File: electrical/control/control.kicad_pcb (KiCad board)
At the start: 2 copper layers, 43 parts, among them J1 USB4105-GF-A, J2 SWD, J3 TC2030-NL, J4 UART, J5 QWIIC, SW1 SYS, U1 USBLC6-2P6, U2 LP5912-3.3DRV, U3 W25Q16JVSSIQ, U4 RP2040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

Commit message: More PCB layout
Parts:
- U3: value W25Q16JVSSIQ -> W25Q16JVSNIQ; footprint Package_SO:SOIC-8_5.3x5.3mm_P1.27mm -> Package_SO:SOIC-8_3.9x4.9mm_P1.27mm
- moved J5 37.9 mm to (167.8, 82.8)
- moved U5 33.3 mm to (166.6, 95.8)
- moved C18 33.3 mm to (166.1, 88.8)
- moved R8 30.6 mm to (161.4, 74.3), turned to 90 degrees
- moved H1 30.0 mm to (137.6, 95.4)
- moved D1 29.2 mm to (161.6, 68.8)
- moved J2 25.7 mm to (135.8, 71.2)
- moved J4 25.0 mm to (142.7, 71.2)
- moved J3 23.4 mm to (136.6, 81.5)
- moved SW1 21.4 mm to (168.8, 71.4)
- moved C15 12.2 mm to (143.9, 78.2), turned to 90 degrees
- moved Y1 7.10 mm to (147.8, 99.4), turned to -90 degrees
- moved C16 6.67 mm to (150.0, 98.6), turned to 90 degrees
- moved U3 6.53 mm to (145.8, 83.0), turned to 90 degrees
- moved C17 3.81 mm to (150.0, 100.6), turned to -90 degrees
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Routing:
- net +3.3V: track 18.2 -> 59.2 mm
- net GND: track 15.6 -> 44.4 mm, vias 11 -> 20
- net /QSPI_SD3: track 0.00 -> 16.0 mm
- net /QSPI_SCLK: track 0.00 -> 13.8 mm
- net /QSPI_SD0: track 0.00 -> 9.72 mm
- net /QSPI_SS: track 0.00 -> 7.59 mm
- net /QSPI_SD1: track 0.00 -> 6.82 mm
- net /QSPI_SD2: track 0.00 -> 5.93 mm
- net Net-(U4-XIN): track 2.94 -> 7.61 mm
- net Net-(C17-Pad1): track 0.00 -> 2.51 mm
- net Net-(U4-XOUT): track 2.50 -> 3.70 mm
- net Net-(U4-GPIO1): track 2.98 -> 1.90 mm
- net Net-(U4-GPIO0): track 2.65 -> 1.65 mm
- net Net-(U4-SWCLK): track 6.05 -> 5.40 mm
- net Net-(U4-SWD): track 5.03 -> 4.47 mm
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- added copper zone on B.Cu, net GND

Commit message: More PCB work
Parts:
- U3: value W25Q16JVSNIQ -> W25Q16JVUXIQ; footprint Package_SO:SOIC-8_3.9x4.9mm_P1.27mm -> Package_SON:Winbond_USON-8-1EP_3x2mm_P0.5mm_EP0.2x1.6mm
- moved J4 39.1 mm to (166.7, 102.1), turned to 90 degrees
- moved J2 39.1 mm to (166.7, 95.1), turned to 90 degrees
- moved H1 32.1 mm to (166.6, 81.6)
- moved J3 30.7 mm to (166.5, 88.2), turned to 0 degrees
- moved J5 27.8 mm to (164.5, 110.4), turned to 0 degrees
- moved C18 21.7 mm to (159.0, 109.3), turned to 90 degrees
- moved U5 20.2 mm to (152.0, 109.7), turned to -90 degrees
- moved R8 17.7 mm to (157.0, 91.4), turned to 0 degrees
- moved R4 12.7 mm to (157.0, 96.6)
- moved R5 11.7 mm to (157.0, 95.6)
- moved C15 5.60 mm to (145.4, 83.6), turned to -90 degrees
- moved D1 3.50 mm to (162.8, 72.1)
- moved R10 3.01 mm to (154.0, 98.6), turned to -90 degrees
- moved R11 2.33 mm to (155.0, 98.6), turned to -90 degrees
- moved SW1 2.30 mm to (171.0, 70.8)
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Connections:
- R4 pad 1: UART_TX -> Net-(U4-GPIO16)
- R4 pad 2: Net-(U4-GPIO0) -> UART_TX
- R5 pad 1: UART_RX -> Net-(U4-GPIO17)
- R5 pad 2: Net-(U4-GPIO1) -> UART_RX
- R8 pad 1: Net-(U4-GPIO2) -> Net-(U4-GPIO25)
- SW1 pad 1: Net-(U4-GPIO3) -> Net-(U4-GPIO24)
- U4 pad 12: unconnected-(U4-GPIO9-Pad12) -> PRESSURE_INT
- U4 pad 13: unconnected-(U4-GPIO10-Pad13) -> I2C_SDA
- U4 pad 14: unconnected-(U4-GPIO11-Pad14) -> I2C_SCL
- U4 pad 2: Net-(U4-GPIO0) -> unconnected-(U4-GPIO0-Pad2)
- U4 pad 27: unconnected-(U4-GPIO16-Pad27) -> Net-(U4-GPIO16)
- U4 pad 28: unconnected-(U4-GPIO17-Pad28) -> Net-(U4-GPIO17)
- U4 pad 3: Net-(U4-GPIO1) -> unconnected-(U4-GPIO1-Pad3)
- U4 pad 36: unconnected-(U4-GPIO24-Pad36) -> Net-(U4-GPIO24)
- U4 pad 37: unconnected-(U4-GPIO25-Pad37) -> Net-(U4-GPIO25)
- U4 pad 38: I2C_SCL -> unconnected-(U4-GPIO26_ADC0-Pad38)
- U4 pad 39: I2C_SDA -> unconnected-(U4-GPIO27_ADC1-Pad39)
- U4 pad 4: Net-(U4-GPIO2) -> unconnected-(U4-GPIO2-Pad4)
- U4 pad 40: PRESSURE_INT -> unconnected-(U4-GPIO28_ADC2-Pad40)
- U4 pad 5: Net-(U4-GPIO3) -> unconnected-(U4-GPIO3-Pad5)
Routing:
- net I2C_SDA: track 0.00 -> 46.7 mm
- net +3.3V: track 59.2 -> 99.7 mm, vias 0 -> 4
- net I2C_SCL: track 0.00 -> 38.5 mm
- net PRESSURE_INT: track 0.00 -> 33.7 mm
- net Net-(U4-GPIO24): track 0.00 -> 21.1 mm
- net Net-(D1-A): track 0.00 -> 18.5 mm
- net +1V1: track 8.33 -> 20.5 mm, vias 0 -> 3
- net /QSPI_SD3: track 16.0 -> 10.6 mm
- net GND: track 44.4 -> 49.4 mm, vias 20 -> 24
- net /QSPI_SCLK: track 13.8 -> 9.16 mm
- net Net-(U4-GPIO16): track 0.00 -> 3.22 mm
- net /QSPI_SS: track 7.59 -> 4.58 mm
- net /QSPI_SD0: track 9.72 -> 6.85 mm
- net Net-(U4-SWCLK): track 5.40 -> 2.95 mm
- net /QSPI_SD1: track 6.82 -> 4.48 mm
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- added copper zone on F.Cu, net +3.3V

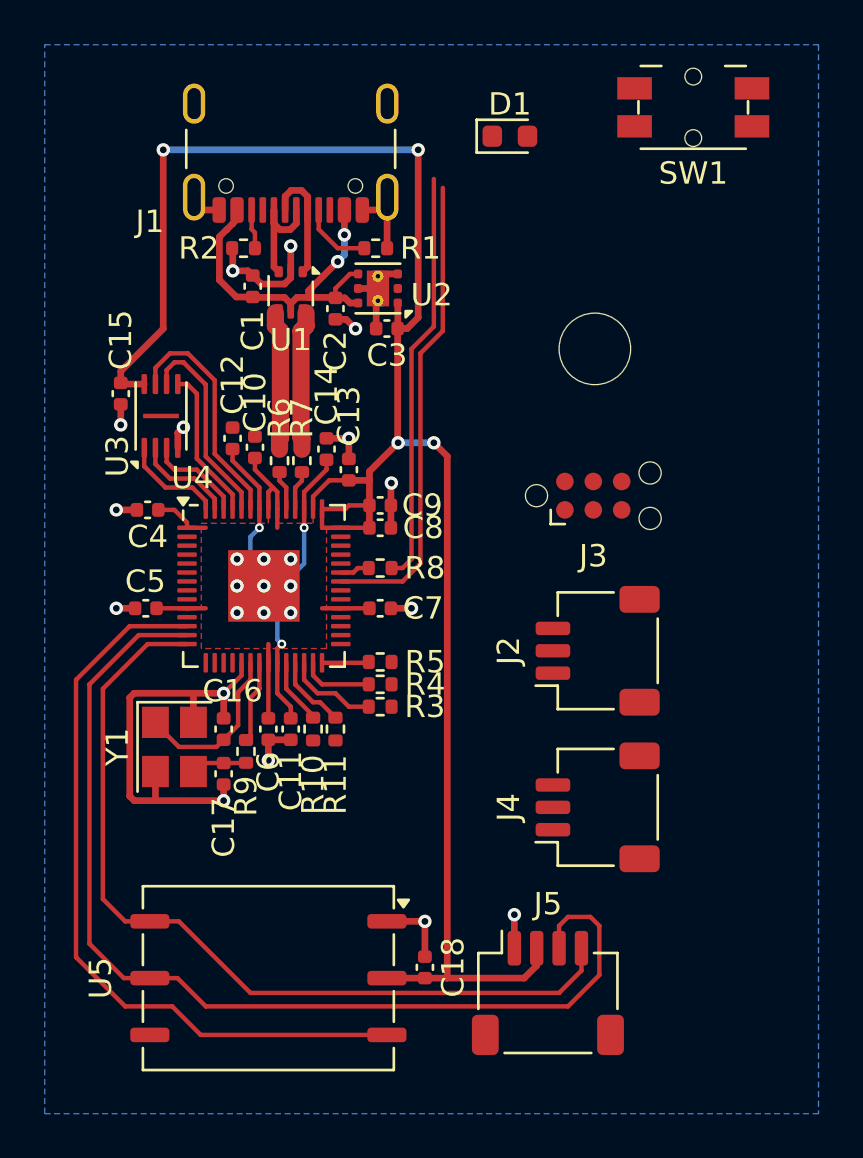
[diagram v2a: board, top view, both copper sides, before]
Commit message: All nets routed for control board
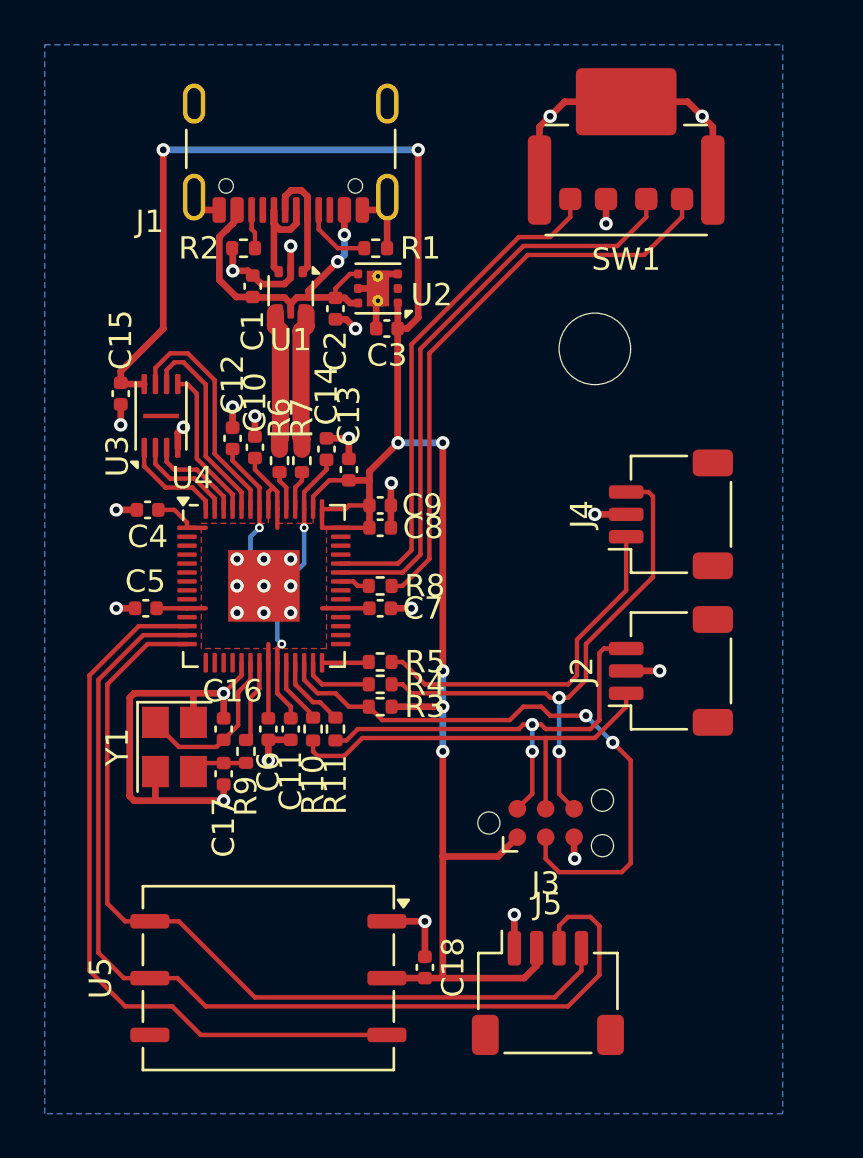
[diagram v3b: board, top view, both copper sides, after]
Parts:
- removed D1: RED, LED_SMD:LED_0603_1608Metric
- SW1: value SYS -> 228EMSARGFR; footprint Button_Switch_SMD:Panasonic_EVQPUL_EVQPUC -> midi_concertina:CTS_228EMS
- moved J3 14.8 mm to (164.4, 102.8)
- moved J4 13.5 mm to (170.0, 89.0)
- moved SW1 5.08 mm to (168.0, 74.9), turned to 180 degrees
- moved J2 3.40 mm to (170.0, 96.0)
- moved R8 0.80 mm to (157.0, 92.2)
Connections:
- R8 pad 1: Net-(U4-GPIO25) -> Net-(U4-GPIO24)
- R8 pad 2: Net-(D1-A) -> Net-(R8-Pad2)
- U4 pad 38: unconnected-(U4-GPIO26_ADC0-Pad38) -> Net-(U4-GPIO26_ADC0)
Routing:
- net Net-(R8-Pad2): track 0.00 -> 26.0 mm
- net UART_TX: track 0.00 -> 25.2 mm, vias 0 -> 2
- net Net-(U4-GPIO25): track 1.34 -> 26.4 mm
- net RUN: track 4.15 -> 27.1 mm, vias 0 -> 2
- net Net-(U4-GPIO26_ADC0): track 0.00 -> 22.9 mm
- net SWDIO: track 0.00 -> 20.7 mm, vias 0 -> 2
- net GND: track 49.4 -> 69.6 mm, vias 24 -> 32
- net Net-(U4-GPIO24): track 21.1 -> 1.34 mm
- net SWCLK: track 0.00 -> 19.2 mm
- net Net-(D1-A): track 18.5 -> 0.00 mm
- net UART_RX: track 0.00 -> 16.0 mm
- net +3.3V: track 99.7 -> 105.9 mm, vias 4 -> 7
- net PRESSURE_INT: track 33.7 -> 33.0 mm

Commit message: Fix various DRC errors
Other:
- board outline added: 33 x 48 mm
- rule solder_mask_min_width: 0.2 -> 0.1
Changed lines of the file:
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@@
 		)
 		(pad_to_mask_clearance 0.038)
-		(solder_mask_min_width 0.2)
+		(solder_mask_min_width 0.1)
 		(allow_soldermask_bridges_in_footprints no)
 		(tenting front back)
@@
 		)
 	)
+	(gr_rect
+		(start 142 68)
+		(end 175 116)
+		(stroke
+			(width 0.05)
+			(type default)
+		)
+		(fill no)
+		(layer "Edge.Cuts")
+	)
 	(segment
 		(start 155.65 78.25)
@@
 		(polygon
 			(pts
-				(xy 142 68) (xy 175 68) (xy 175 115.8) (xy 142 115.8)
+				(xy 142 68) (xy 175 68) (xy 175 116) (xy 142 116)
 			)
 		)

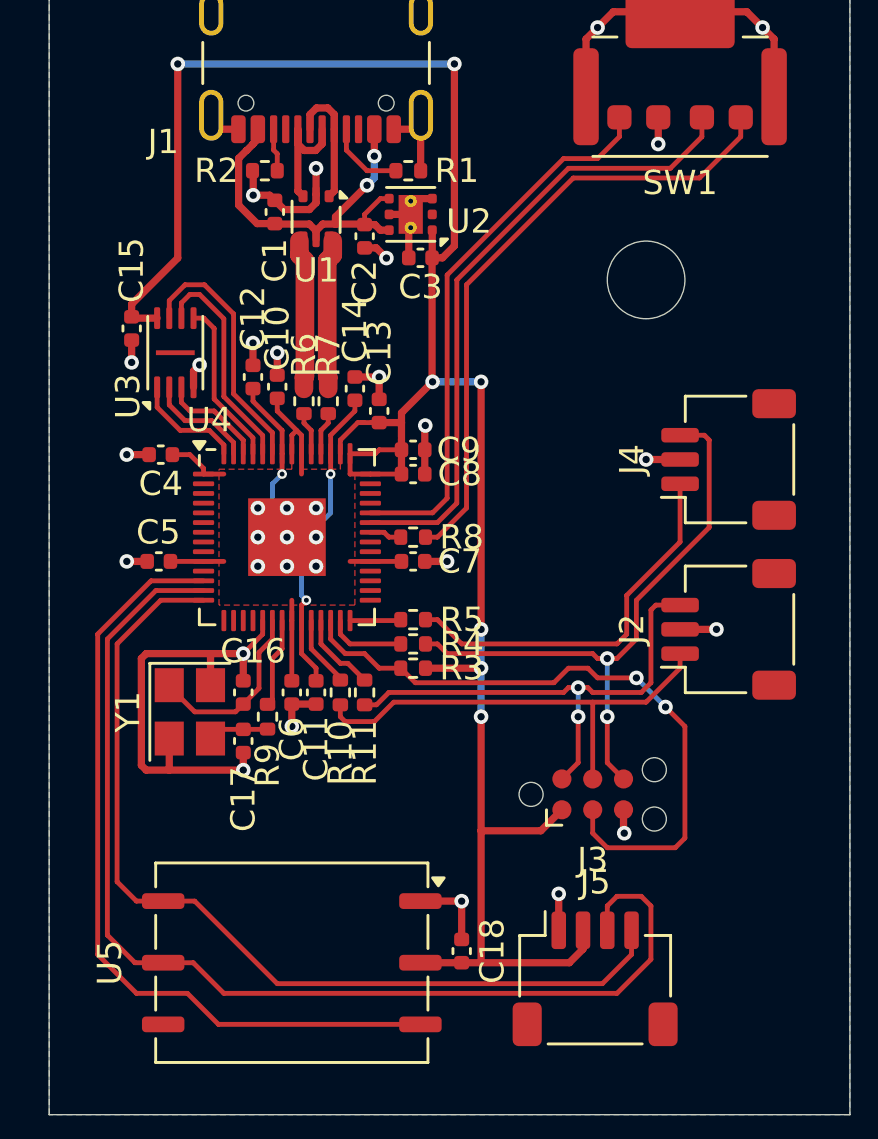
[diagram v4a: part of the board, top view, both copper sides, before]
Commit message: Clean up silkscreen
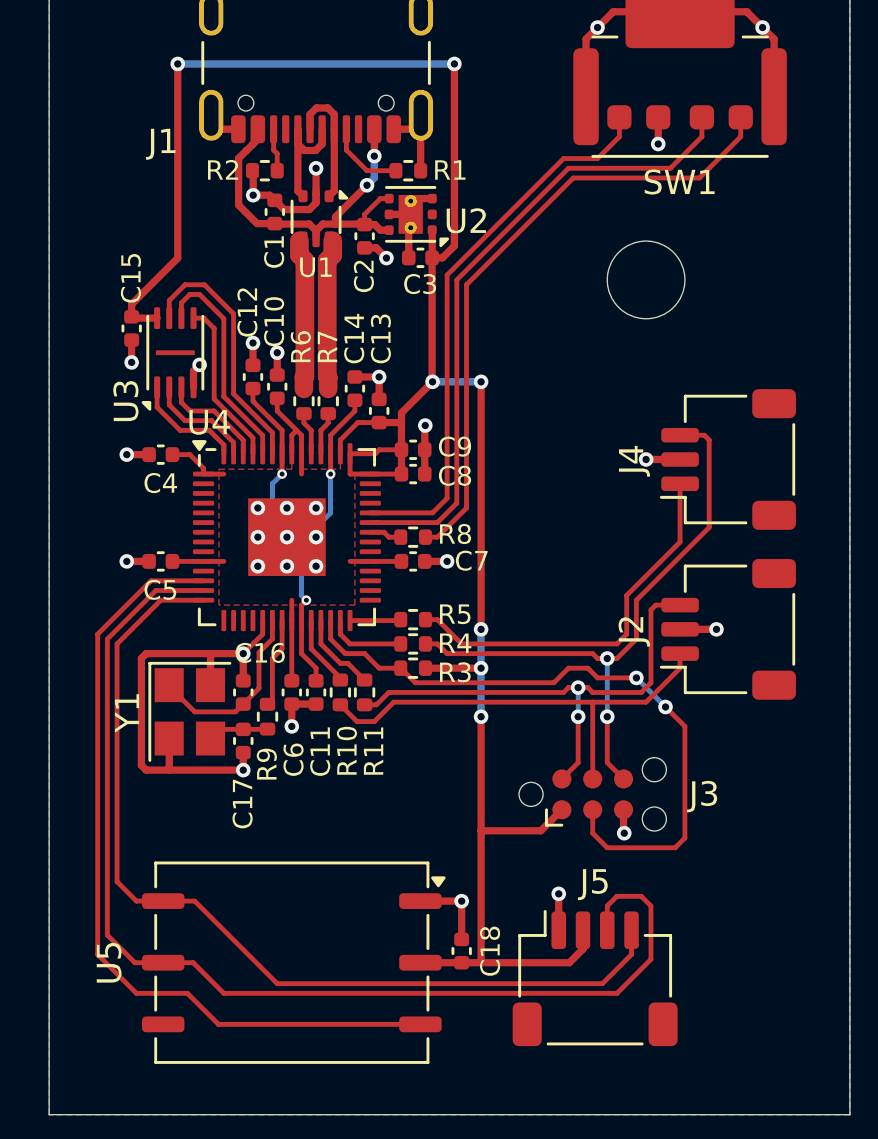
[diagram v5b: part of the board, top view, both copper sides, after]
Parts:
- moved C5 0.08 mm to (146.6, 93.2)

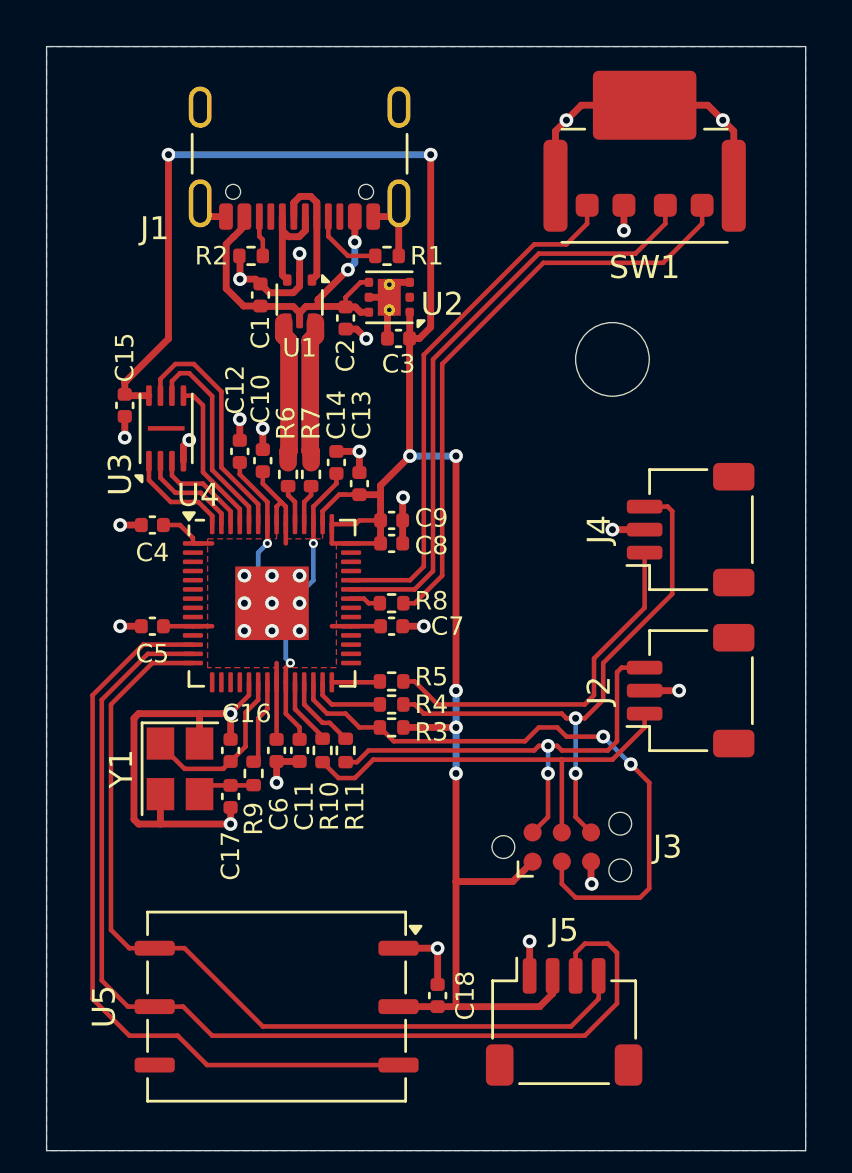
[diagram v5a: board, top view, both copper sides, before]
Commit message: Fix via sizes
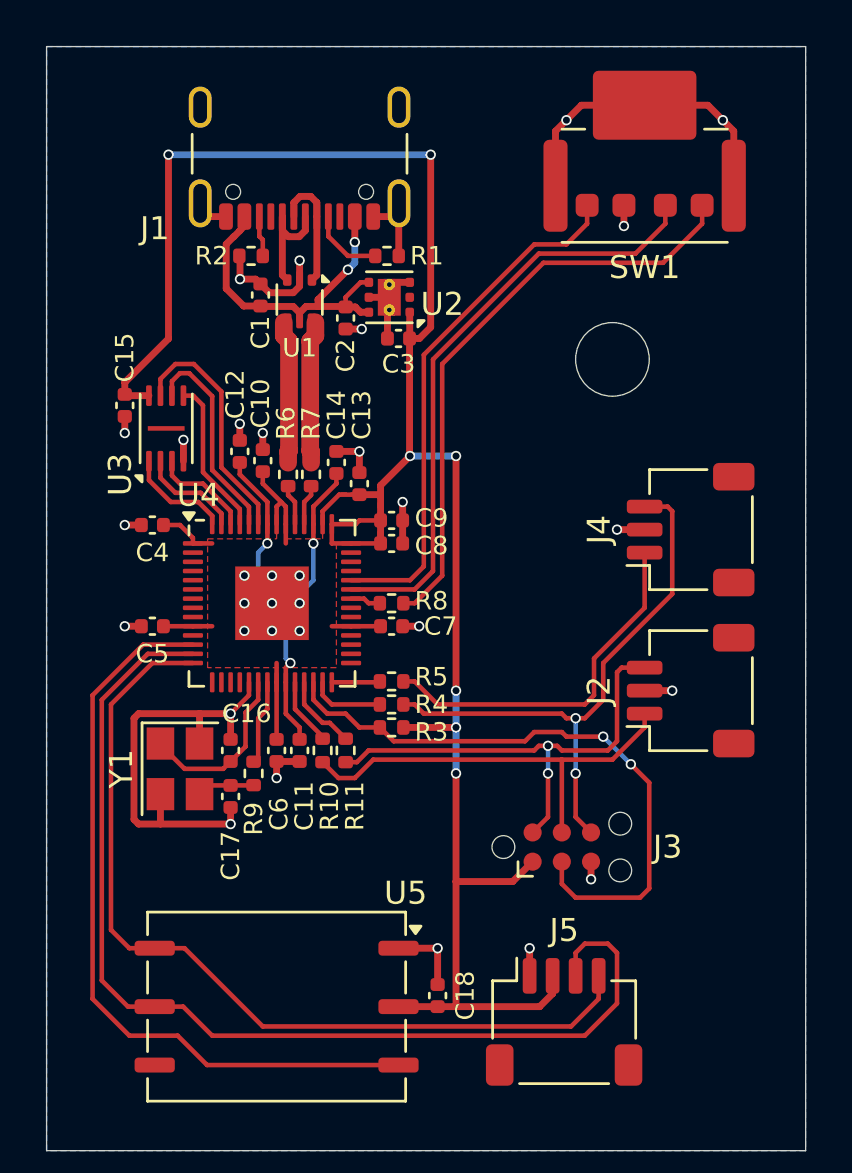
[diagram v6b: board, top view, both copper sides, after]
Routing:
- net GND: track 69.7 -> 66.1 mm
